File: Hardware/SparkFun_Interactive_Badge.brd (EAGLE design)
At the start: 17.8 x 77.5 mm, 34 parts, among them Q1 DMG2307L, U1 MIC5205-3.3V, U2 ATMEGA328P, U3 CY7C65213

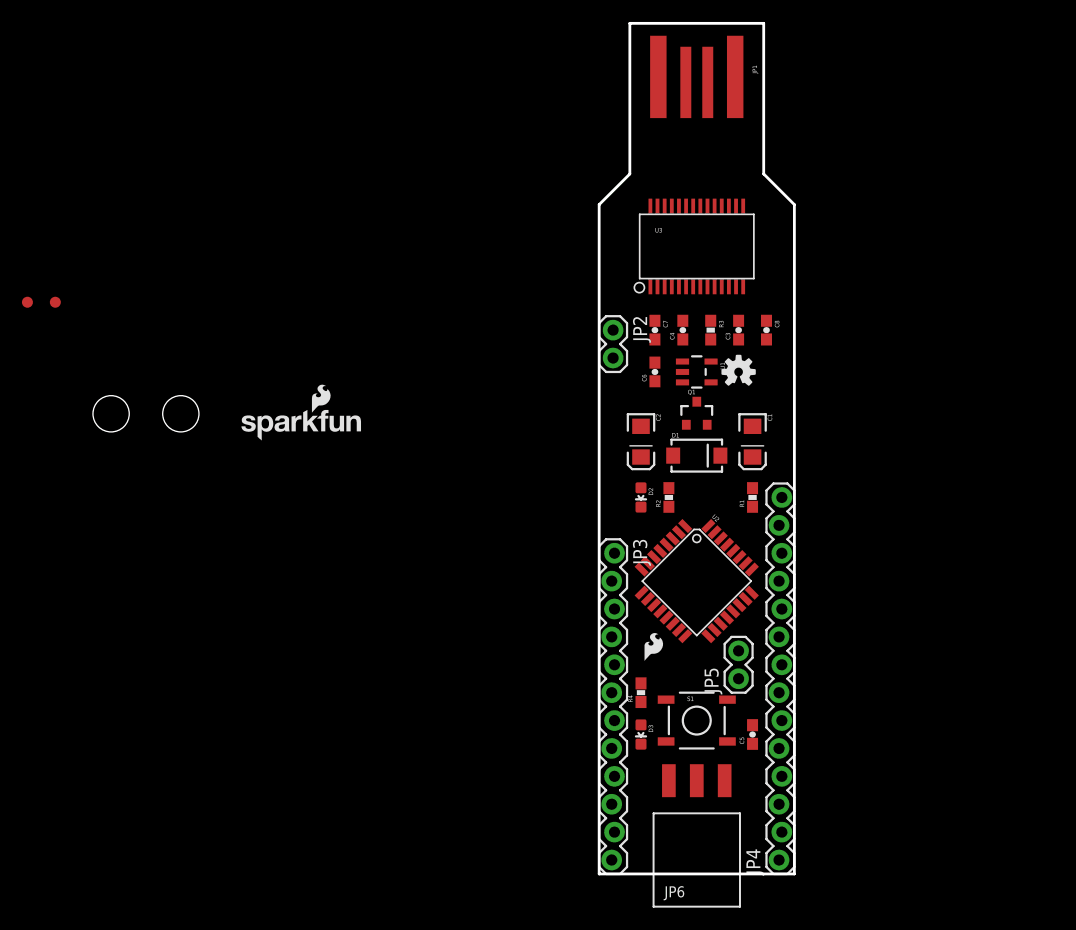
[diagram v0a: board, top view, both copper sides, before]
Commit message: Added PTH UART header on bottom. Added outline of wing on tDocu layer.
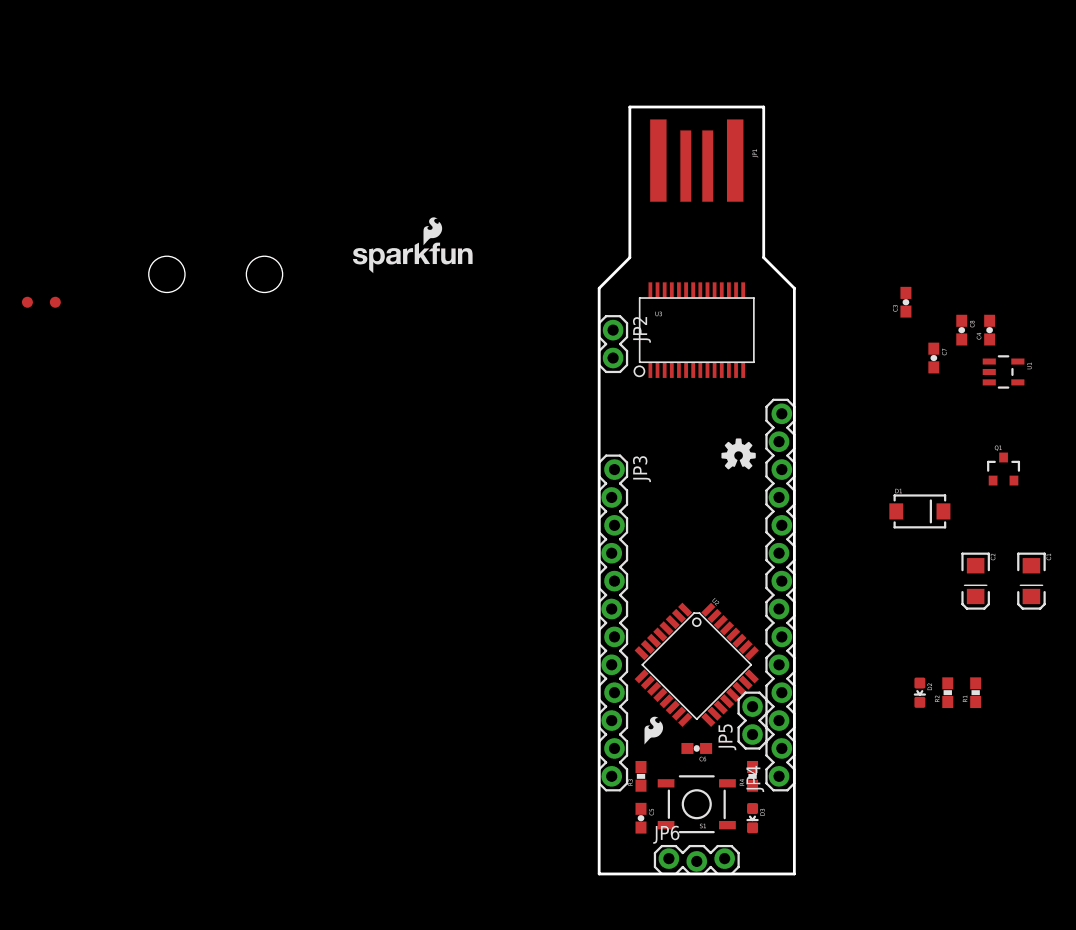
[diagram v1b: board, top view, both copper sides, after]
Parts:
- JP6: value 1x3 RA Female .1" -> M03LOCK Female; device SparkFun-Connectors:1X03_SMD_RA_FEMALE -> SparkFun-Connectors:1X03_LOCK
- S1: value SWITCH-MOMENTARY-2SMD -> SWITCH-MOMENTARY-2SMD-REDUNDANT
- moved R3 41.1 mm to (3.81, 8.89), turned to 90 degrees
- moved C6 34.5 mm to (8.89, 11.4), turned to 180 degrees
- moved C2 33.0 mm to (34.3, 26.7)
- moved D2 31.0 mm to (29.2, 16.5)
- moved R2 31.0 mm to (31.8, 16.5)
- moved C1 28.4 mm to (39.4, 26.7)
- moved Q1 28.4 mm to (36.8, 36.8)
- moved C4 27.9 mm to (35.6, 49.5)
- moved U1 27.9 mm to (36.8, 45.7)
- moved R1 27.0 mm to (34.3, 16.5)
- moved C7 25.5 mm to (30.5, 47.0)
- moved D1 20.9 mm to (29.2, 33.0)
- moved U$1 18.3 mm to (-22.9, 54.6)
- moved FRAME1 18.3 mm to (-87.6, 0.00)
- moved C8 17.8 mm to (33.0, 49.5)
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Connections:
- net GND: now also S1.2
- net RESET: now also S1.4
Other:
- board size 17.8 x 77.5 mm -> 17.8 x 69.8 mm

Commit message: Initial layout complete
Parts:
- JP2, JP5: value M02PTH -> M021X02_NO_SILK; device SparkFun-Connectors:1X02 -> SparkFun-Connectors:1X02_NO_SILK
- JP3: value M12LOCK -> M13LOCK_NO_SILK; device SparkFun-Connectors:1X12_LOCK -> SparkFun-Connectors:1X13_LOCK_NO_SILK
- JP4: value M14LOCK -> M15LOCK_NO_SILK; device SparkFun-Connectors:1X14_LOCK -> SparkFun-Connectors:1X15_LOCK_NO_SILK
- JP6: device SparkFun-Connectors:1X03_LOCK -> SparkFun-Connectors:1X03_LOCK_NO_SILK
- moved STANDOFF1 72.7 mm to (20.3, 2.54)
- moved FRAME1 69.3 mm to (-19.1, -10.2)
- moved STANDOFF2 63.8 mm to (-2.54, 2.54)
- moved LOGO2 36.3 mm to (15.9, 1.91)
- moved R2 33.3 mm to (6.35, 38.1)
- moved JP4 33.0 mm to (16.5, 41.9), turned to 270 degrees
- moved C3 32.3 mm to (5.08, 29.2), turned to 270 degrees
- moved R1 30.7 mm to (5.08, 26.0)
- moved JP3 30.5 mm to (1.27, 6.35), turned to 90 degrees
- moved U1 30.2 mm to (8.89, 34.3), turned to 90 degrees
- moved C2 30.0 mm to (5.08, 33.7)
- moved D2 29.6 mm to (8.89, 38.1), turned to 0 degrees
- moved Q1 29.0 mm to (8.89, 29.2)
- moved C7 28.0 mm to (2.54, 45.1)
- moved C1 27.6 mm to (12.7, 33.7), turned to 90 degrees
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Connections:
- removed net N$10: JP3.6
- removed net N$11: JP3.5
- removed net N$12: JP3.4
- removed net N$13: JP3.3
- removed net N$14: JP3.2
- removed net N$15: JP3.1
- removed net N$16: JP4.1
- removed net N$17: JP4.2
- removed net N$18: JP4.3
- removed net N$19: JP4.4
- removed net N$20: JP4.5
- removed net N$21: JP4.6
- removed net N$22: JP4.7
- removed net N$23: JP4.8
- removed net N$24: JP4.9
- removed net N$25: JP4.10
- removed net N$26: JP4.11
- removed net N$27: JP4.12
- removed net N$28: JP4.13
- removed net N$29: JP4.14
- removed net N$3: JP3.12
- removed net N$30: JP5.2
- removed net N$31: JP5.1
- removed net N$5: JP3.11
- removed net N$6: JP3.10
- removed net N$7: JP3.9
- removed net N$8: JP3.8
- removed net N$9: JP3.7
- net 3.3V: now also JP4.2
- net 5V: now also JP4.1
- net A0: now also JP4.11
- net A1: now also JP4.10
- net A2: now also JP4.9
- net A3: now also JP4.8
- net A4: now also JP4.7
- net A5: now also JP4.6
- net A6: now also JP5.1
- net A7: now also JP5.2
- net D10: now also JP4.15, JP6.1
- net D2: now also JP3.8
- net D3: now also JP3.7
- net D4: now also JP3.6
- net D5: now also JP3.5
- net D6: now also JP3.4
- net D7: now also JP3.3
- net D8: now also JP3.2
- net D9: now also JP3.1
- net DTR: now also JP3.13
- net GND: now also JP3.9, JP4.3, JP6.2
- net MISO: now also JP4.13
- net MOSI: now also JP4.14, JP6.3
- net RESET: now also JP3.10, JP4.4
- net RXI: now also JP3.11
- net SCK: now also JP4.12
- net TXO: now also JP3.12
- net VCC: now also JP4.5
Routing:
- net RESET: track 0.00 -> 76.2 mm, vias 0 -> 3
- net 3.3V: track 0.00 -> 51.9 mm, vias 0 -> 2
- net 5V: track 0.00 -> 48.4 mm
- net VCC: track 0.00 -> 45.7 mm
- net RXI: track 0.00 -> 38.0 mm, vias 0 -> 1
- net TXO: track 0.00 -> 33.1 mm, vias 0 -> 2
- net D10: track 0.00 -> 28.1 mm, vias 0 -> 1
- net MOSI: track 0.00 -> 28.1 mm, vias 0 -> 1
- net DTR: track 0.00 -> 26.5 mm
- net AREF: track 0.00 -> 24.8 mm, vias 0 -> 2
- net VBAT: track 0.00 -> 20.6 mm, vias 0 -> 1
- net MISO: track 0.00 -> 19.7 mm, vias 0 -> 1
- net SCK: track 0.00 -> 14.9 mm
- net D3: track 0.00 -> 12.7 mm, vias 0 -> 1
- net D9: track 0.00 -> 12.6 mm, vias 0 -> 1
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- added copper zone on layer 1, net GND
- added copper zone on layer 16, net GND
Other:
- board size 17.8 x 69.8 mm -> 17.8 x 63.5 mm
- board text added: "Shawn Hymel"

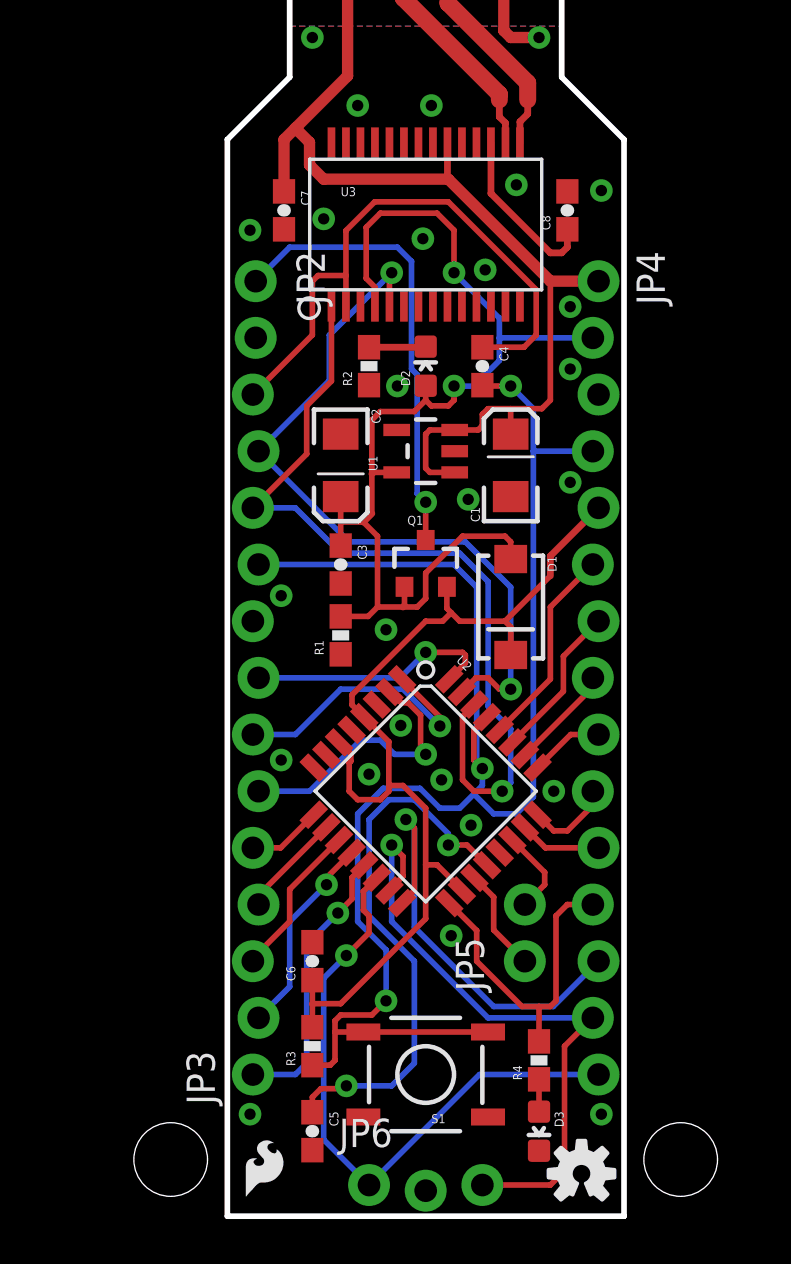
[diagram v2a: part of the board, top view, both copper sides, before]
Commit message: Added mounting holes in brd. Still need to fix 2 air wires.
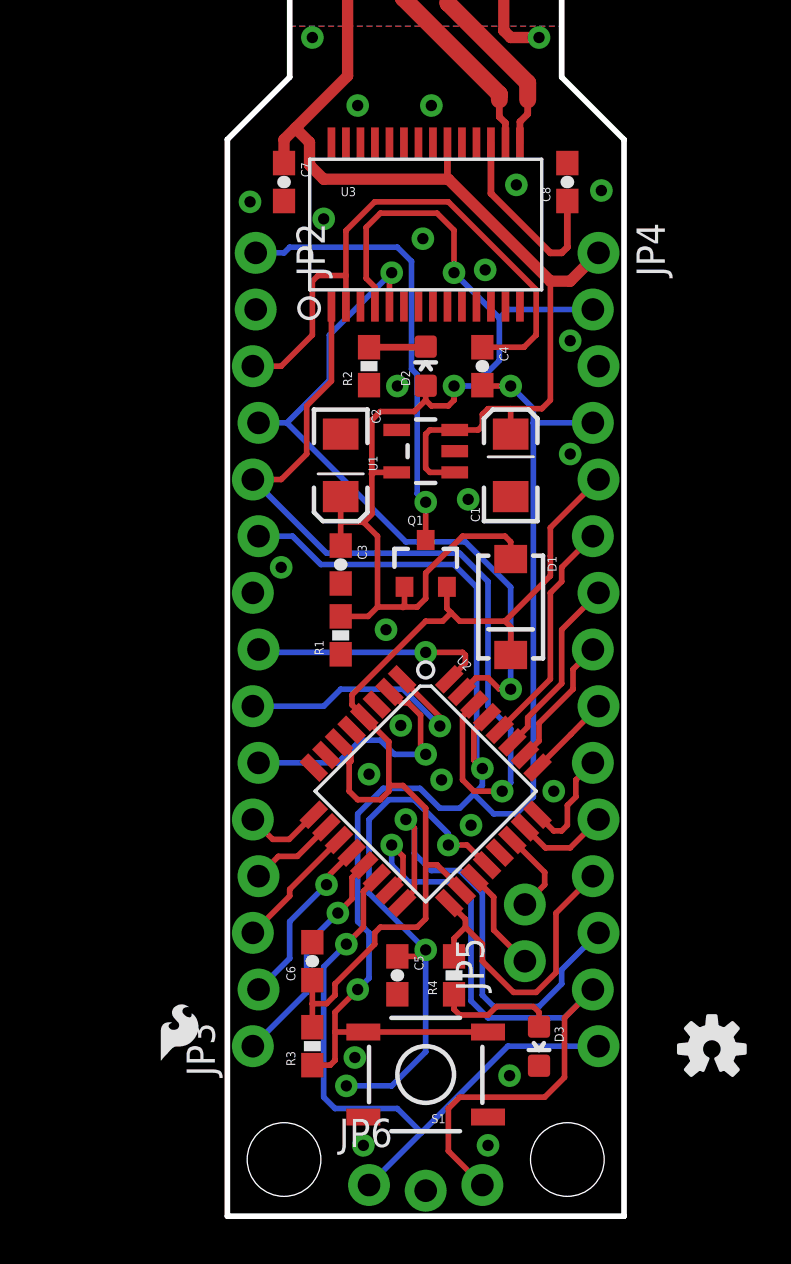
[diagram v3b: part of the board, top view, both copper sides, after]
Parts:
- moved LOGO2 8.08 mm to (21.7, 7.49)
- moved C5 7.96 mm to (7.62, 10.8)
- moved LOGO1 7.19 mm to (-3.30, 6.60)
- moved R4 5.39 mm to (10.2, 10.8)
- moved STANDOFF1 5.08 mm to (15.2, 2.54)
- moved STANDOFF2 5.08 mm to (2.54, 2.54)
- moved D3 3.81 mm to (14.0, 7.62)
- moved JP2 1.27 mm to (1.27, 43.2)
- moved JP4 1.27 mm to (16.5, 43.2)
- moved JP3 1.27 mm to (1.27, 7.62)
- moved C7 1.27 mm to (2.54, 46.4)
- moved C8 1.27 mm to (15.2, 46.4)
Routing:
- net MOSI: track 28.1 -> 32.8 mm
- net N$1: track 1.45 -> 5.50 mm
- net D9: track 12.6 -> 10.2 mm
- net VCC: track 45.7 -> 47.5 mm
- net MISO: track 19.7 -> 21.3 mm
- net TXO: track 33.1 -> 31.8 mm
- net N$2: track 7.70 -> 8.97 mm
- net A4: track 7.03 -> 8.30 mm
- net D8: track 9.14 -> 7.87 mm
- net D7: track 7.03 -> 5.76 mm
- net A5: track 9.14 -> 10.4 mm
- net A3: track 4.72 -> 5.99 mm
- net A1: track 3.89 -> 5.01 mm
- net RESET: track 76.2 -> 75.3 mm
- net SCK: track 14.9 -> 14.0 mm
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
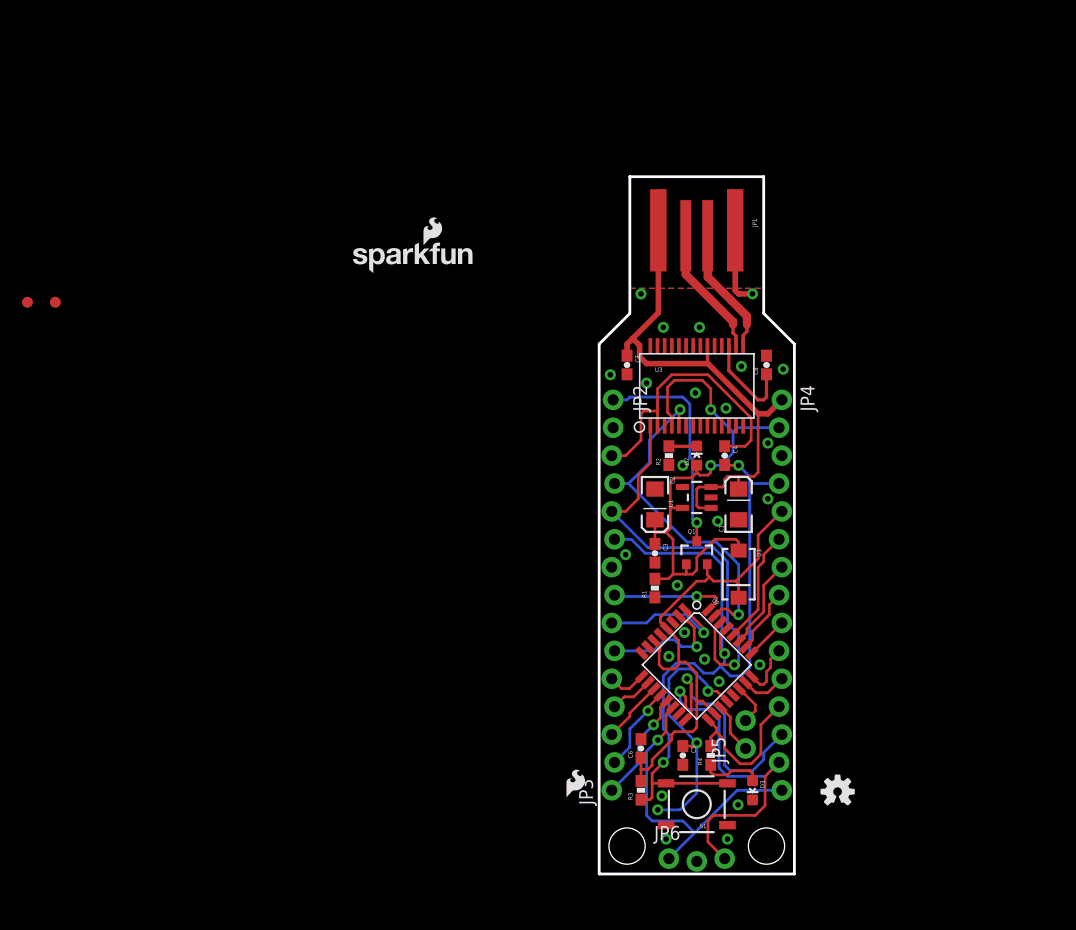
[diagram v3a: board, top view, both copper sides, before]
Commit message: Finished layout. Need to move some components to accomodate silk numbers.
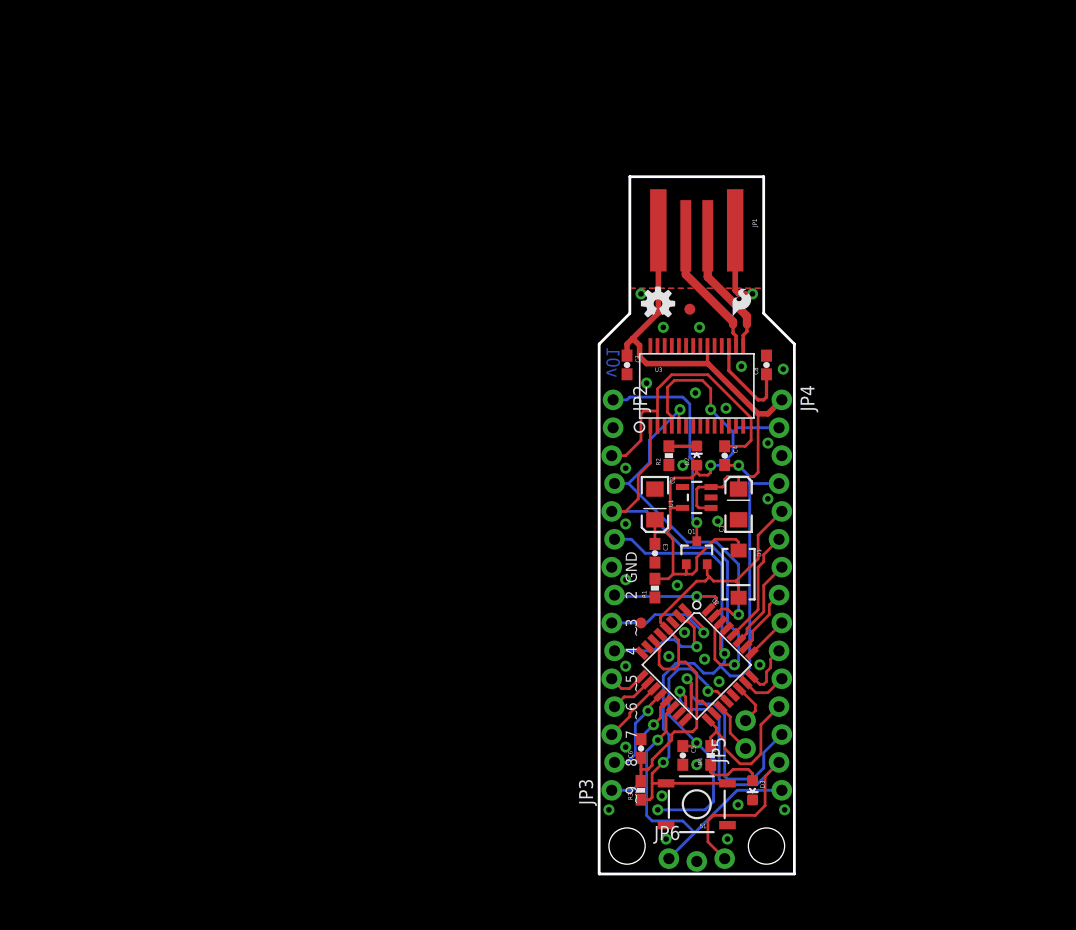
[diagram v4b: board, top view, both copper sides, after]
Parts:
- moved FID1 60.8 mm to (3.81, 22.9)
- moved FID2 60.3 mm to (8.26, 51.4)
- moved LOGO2 47.4 mm to (5.36, 51.9)
- moved LOGO1 46.4 mm to (11.8, 50.4)
- moved U$1 38.8 mm to (14.9, 45.7), flipped to the bottom
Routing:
- net AREF: track 24.2 -> 26.8 mm
- net MISO: track 21.3 -> 23.0 mm
- net MOSI: track 32.8 -> 34.0 mm
- net D9: track 10.2 -> 11.3 mm
- net D8: track 7.87 -> 8.54 mm
- net GND: vias 25 -> 31
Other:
- board text added: "2"
- board text added: "3"
- board text added: "4"
- board text added: "5"
- board text added: "6"
- board text added: "7"
- board text added: "8"
- board text added: "9"
- board text added: "GND"
- board text added: "v01"
- board text added: "~"
